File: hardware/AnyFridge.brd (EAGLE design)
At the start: 160 x 100 mm, 7 parts, among them U1 TSSP77038TT

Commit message: updated board
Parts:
- removed ESP1: ESP32, ESP32:ESP32
- removed LED1: WP154A4SUREQBFZGC, MISC-PARTS:LED4_WP154A4SUREQBFZGC_KNB
- removed S1: TS04-66-73-BK-100-SMT, MISC-PARTS:SW_TS04-66-73-BK-100-SMT
- removed SEN-1: SEN-18088, SEN-18088:SEN-18088
- removed U1: TSSP77038TT, MISC-PARTS:TSSP77038TT
- added ESP-1: ESP32, ESP32:ESP32
- added LED-1: WP154A4SUREQBFZGC, MISC-PARTS:LED4_WP154A4SUREQBFZGC_KNB
- added SCAN-1: SEN-18088, SEN-18088:SEN-18088
- added SENS-1: TSSP77038TT, MISC-PARTS:TSSP77038TT
- added SWITCH-1: TS04-66-73-BK-100-SMT, MISC-PARTS:SW_TS04-66-73-BK-100-SMT
- moved FRAME1 135.5 mm to (43.2, 2.54)
- moved R1 52.1 mm to (49.5, 3.81), turned to 0 degrees
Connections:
- removed net BUTTON: ESP1.15, S1.3
- removed net OUT: ESP1.13, U1.3
- removed net RX0: ESP1.19, SEN-1.RX
- removed net TX0: ESP1.22, SEN-1.TX
- new net RX1: ESP-1.16, SCAN-1.TX
- new net SENS-OUT: ESP-1.13, SENS-1.3
- new net SWI-OUT: ESP-1.15, SWITCH-1.3
- new net TX1: ESP-1.17, SCAN-1.RX
- net 3.3V: now also ESP-1.3V3, SCAN-1.3.3V, SENS-1.2, SWITCH-1.2; no longer ESP1.3V3, S1.2, SEN-1.3.3V, U1.2
- net BLUE: now also ESP-1.12, LED-1.3; no longer ESP1.12, LED1.3
- net GND: now also ESP-1.GND, LED-1.2, SCAN-1.GND, SENS-1.1, SENS-1.4; no longer ESP1.GND, LED1.2, SEN-1.GND, U1.1, U1.4
- net GREEN: now also ESP-1.27, LED-1.4; no longer ESP1.27, LED1.4
- net N$1: now also SWITCH-1.1; no longer S1.1
- net RED: now also ESP-1.33, LED-1.1; no longer ESP1.33, LED1.1
- net STAT: now also ESP-1.23, SCAN-1.STAT; no longer ESP1.23, SEN-1.STAT
- net TRIG: now also ESP-1.21, SCAN-1.TRIG; no longer ESP1.21, SEN-1.TRIG
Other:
- board size 160 x 100 mm -> 100 x 80 mm

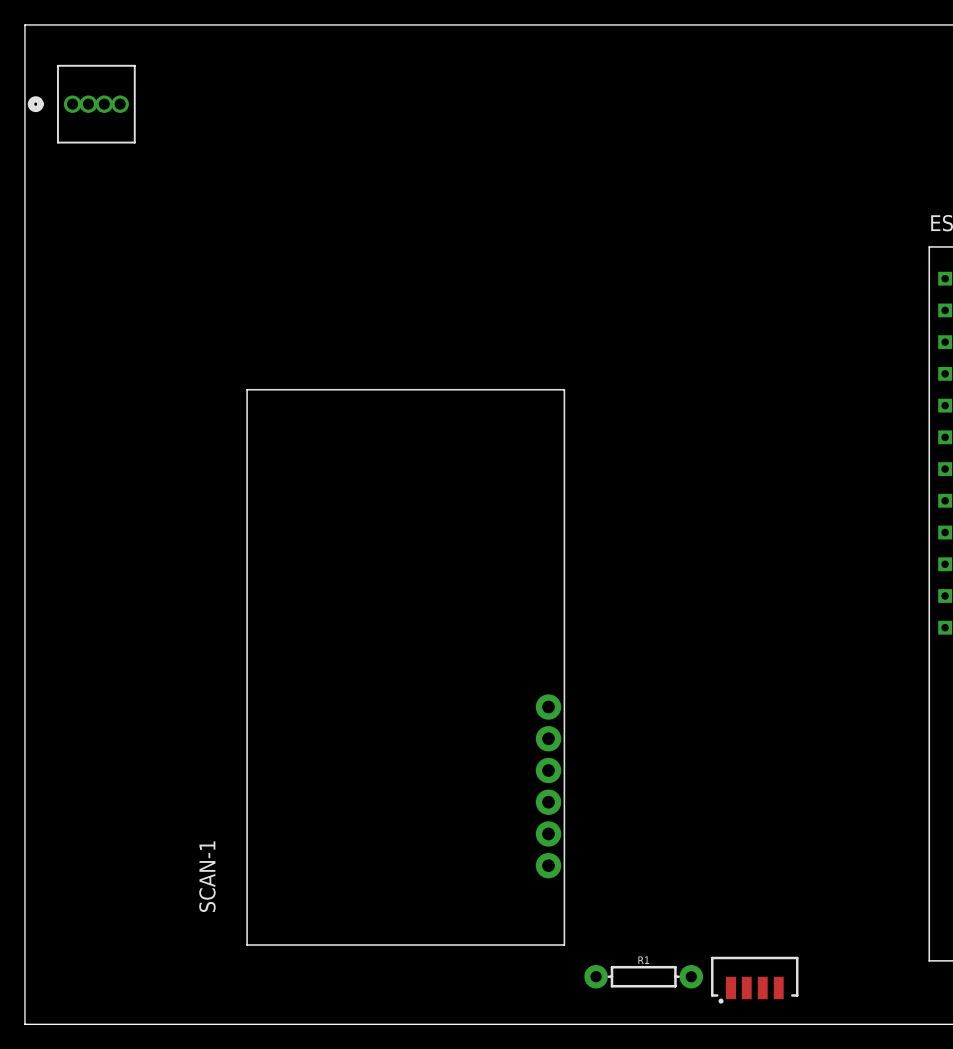
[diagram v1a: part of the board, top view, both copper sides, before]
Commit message: Rotated barcode scanner
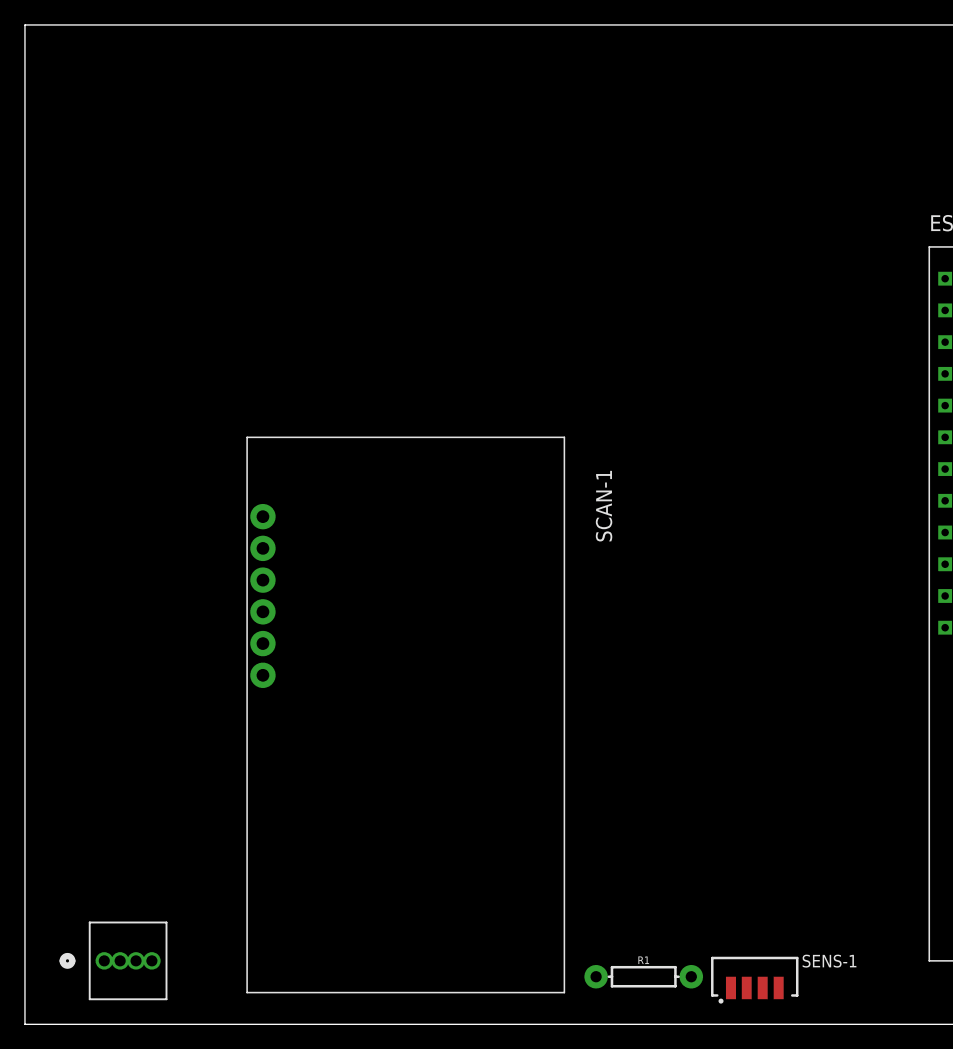
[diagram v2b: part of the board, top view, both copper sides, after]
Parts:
- moved LED-1 68.6 mm to (6.35, 5.08)
- moved SCAN-1 47.9 mm to (43.2, 47.0), turned to 270 degrees
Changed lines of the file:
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@@
 <attribute name="VERSION" value="v01" x="85.09" y="-149.86" size="1.778" layer="27" display="off"/>
 </element>
-<element name="LED-1" library="MISC-PARTS" package="LED4_WP154A4SUREQBFZGC_KNB" value="WP154A4SUREQBFZGC" x="3.81" y="73.66" smashed="yes">
-<attribute name="COPYRIGHT" value="Copyright (C) 2025 Ultra Librarian. All rights reserved." x="38.1" y="-62.23" size="1.778" layer="27" display="off"/>
-<attribute name="MANUFACTURER_PART_NUMBER" value="WP154A4SUREQBFZGC" x="38.1" y="-62.23" size="1.778" layer="27" display="off"/>
-<attribute name="MFR_NAME" value="Kingbright" x="38.1" y="-62.23" size="1.778" layer="27" display="off"/>
-<attribute name="NAME" x="2.4384" y="73.025" size="1.27" layer="27" ratio="6" rot="SR0"/>
-<attribute name="VALUE" x="3.9878" y="73.025" size="1.27" layer="27" ratio="6" rot="SR0"/>
+<element name="LED-1" library="MISC-PARTS" package="LED4_WP154A4SUREQBFZGC_KNB" value="WP154A4SUREQBFZGC" x="6.35" y="5.08" smashed="yes">
+<attribute name="COPYRIGHT" value="Copyright (C) 2025 Ultra Librarian. All rights reserved." x="40.64" y="-130.81" size="1.778" layer="27" display="off"/>
+<attribute name="MANUFACTURER_PART_NUMBER" value="WP154A4SUREQBFZGC" x="40.64" y="-130.81" size="1.778" layer="27" display="off"/>
+<attribute name="MFR_NAME" value="Kingbright" x="40.64" y="-130.81" size="1.778" layer="27" display="off"/>
+<attribute name="NAME" x="4.9784" y="4.445" size="1.27" layer="27" ratio="6" rot="SR0"/>
+<attribute name="VALUE" x="6.5278" y="4.445" size="1.27" layer="27" ratio="6" rot="SR0"/>
 </element>
 <element name="R1" library="SparkFun-Resistors" library_urn="urn:adsk.eagle:library:532" package="AXIAL-0.3" package3d_urn="urn:adsk.eagle:package:39658/2" value="10k" x="49.53" y="3.81" smashed="yes">
@@
 <attribute name="VALUE" x="49.53" y="2.794" size="0.6096" layer="27" font="vector" ratio="20" align="top-center"/>
 </element>
-<element name="SCAN-1" library="SEN-18088" package="SEN-18088" value="SEN-18088" x="17.78" y="6.35" smashed="yes" rot="R90">
-<attribute name="NAME" x="15.24" y="8.89" size="1.27" layer="25" rot="R90"/>
-<attribute name="VALUE" x="15.24" y="41.91" size="1.27" layer="27" rot="R90"/>
+<element name="SCAN-1" library="SEN-18088" package="SEN-18088" value="SEN-18088" x="43.18" y="46.99" smashed="yes" rot="R270">
+<attribute name="NAME" x="45.72" y="44.45" size="1.27" layer="25" rot="R270"/>
+<attribute name="VALUE" x="45.72" y="11.43" size="1.27" layer="27" rot="R270"/>
 </element>
 <element name="SENS-1" library="MISC-PARTS" package="TSSP77038TT" package3d_urn="urn:adsk.eagle:package:47059864/1" value="TSSP77038TT" x="58.42" y="3.81" smashed="yes">
@@
 <attribute name="MF" value="Vishay" x="85.09" y="-149.86" size="1.778" layer="27" display="off"/>
 <attribute name="MP" value="TSSP77038TT" x="85.09" y="-149.86" size="1.778" layer="27" display="off"/>
+<attribute name="NAME" x="62.17" y="4.56" size="1" layer="51" ratio="21" rot="SR0"/>
 <attribute name="NAME" x="62.17" y="4.56" size="1" layer="25" ratio="20" rot="SR0"/>
-<attribute name="NAME" x="62.17" y="4.56" size="1" layer="51" ratio="21" rot="SR0"/>
 <attribute name="PACKAGE" value="None" x="85.09" y="-149.86" size="1.778" layer="27" display="off"/>
 <attribute name="PRICE" value="None" x="85.09" y="-149.86" size="1.778" layer="27" display="off"/>
@@
 <contactref element="LED-1" pad="2"/>
 <contactref element="R1" pad="P$1"/>
+<wire x1="60.325" y1="2.91" x2="93.98" y2="29.21" width="0" layer="19" extent="1-1"/>
 <wire x1="56.515" y1="2.91" x2="60.325" y2="2.91" width="0" layer="19" extent="1-1"/>
 <wire x1="45.72" y1="3.81" x2="56.515" y2="2.91" width="0" layer="19" extent="1-1"/>
-<wire x1="5.08" y1="73.66" x2="56.515" y2="2.91" width="0" layer="19" extent="1-1"/>
-<wire x1="41.91" y1="12.7" x2="5.08" y2="73.66" width="0" layer="19" extent="1-1"/>
-<wire x1="93.98" y1="29.21" x2="41.91" y2="12.7" width="0" layer="19" extent="1-1"/>
+<wire x1="19.05" y1="40.64" x2="45.72" y2="3.81" width="0" layer="19" extent="1-1"/>
+<wire x1="7.62" y1="5.08" x2="19.05" y2="40.64" width="0" layer="19" extent="1-1"/>
 </signal>
 <signal name="3.3V">
@@
 <contactref element="SENS-1" pad="2"/>
 <contactref element="SWITCH-1" pad="2"/>
-<wire x1="76.73" y1="68.87" x2="57.785" y2="2.91" width="0" layer="19" extent="1-1"/>
-<wire x1="41.91" y1="20.32" x2="57.785" y2="2.91" width="0" layer="19" extent="1-1"/>
-<wire x1="93.98" y1="24.13" x2="41.91" y2="20.32" width="0" layer="19" extent="1-1"/>
+<wire x1="93.98" y1="24.13" x2="76.73" y2="68.87" width="0" layer="19" extent="1-1"/>
+<wire x1="57.785" y1="2.91" x2="93.98" y2="24.13" width="0" layer="19" extent="1-1"/>
+<wire x1="19.05" y1="33.02" x2="76.73" y2="68.87" width="0" layer="19" extent="1-1"/>
 </signal>
 <signal name="TRIG">
 <contactref element="SCAN-1" pad="TRIG"/>
 <contactref element="ESP-1" pad="21"/>
-<wire x1="41.91" y1="22.86" x2="93.98" y2="59.69" width="0" layer="19" extent="1-1"/>
+<wire x1="19.05" y1="30.48" x2="93.98" y2="59.69" width="0" layer="19" extent="1-1"/>
 </signal>
 <signal name="STAT">
 <contactref element="SCAN-1" pad="STAT"/>
 <contactref element="ESP-1" pad="23"/>
-<wire x1="41.91" y1="25.4" x2="73.66" y2="59.69" width="0" layer="19" extent="1-1"/>
+<wire x1="19.05" y1="27.94" x2="73.66" y2="59.69" width="0" layer="19" extent="1-1"/>
 </signal>
 <signal name="RED">
 <contactref element="LED-1" pad="1"/>
 <contactref element="ESP-1" pad="33"/>
-<wire x1="73.66" y1="46.99" x2="3.81" y2="73.66" width="0" layer="19" extent="1-1"/>
+<wire x1="73.66" y1="46.99" x2="6.35" y2="5.08" width="0" layer="19" extent="1-1"/>
 </signal>
 <signal name="BLUE">
 <contactref element="LED-1" pad="3"/>
 <contactref element="ESP-1" pad="12"/>
-<wire x1="73.66" y1="41.91" x2="6.35" y2="73.66" width="0" layer="19" extent="1-1"/>
+<wire x1="73.66" y1="41.91" x2="8.89" y2="5.08" width="0" layer="19" extent="1-1"/>
 </signal>
 <signal name="GREEN">
 <contactref element="LED-1" pad="4"/>
 <contactref element="ESP-1" pad="27"/>
-<wire x1="73.66" y1="44.45" x2="7.62" y2="73.66" width="0" layer="19" extent="1-1"/>
+<wire x1="73.66" y1="44.45" x2="10.16" y2="5.08" width="0" layer="19" extent="1-1"/>
 </signal>
 <signal name="N$1">
@@
 <contactref element="ESP-1" pad="17"/>
 <contactref element="SCAN-1" pad="RX"/>
-<wire x1="41.91" y1="15.24" x2="93.98" y2="57.15" width="0" layer="19" extent="1-1"/>
+<wire x1="19.05" y1="38.1" x2="93.98" y2="57.15" width="0" layer="19" extent="1-1"/>
 </signal>
 <signal name="RX1">
 <contactref element="ESP-1" pad="16"/>
 <contactref element="SCAN-1" pad="TX"/>
-<wire x1="41.91" y1="17.78" x2="93.98" y2="54.61" width="0" layer="19" extent="1-1"/>
+<wire x1="19.05" y1="35.56" x2="93.98" y2="54.61" width="0" layer="19" extent="1-1"/>
 </signal>
 <signal name="SWI-OUT">

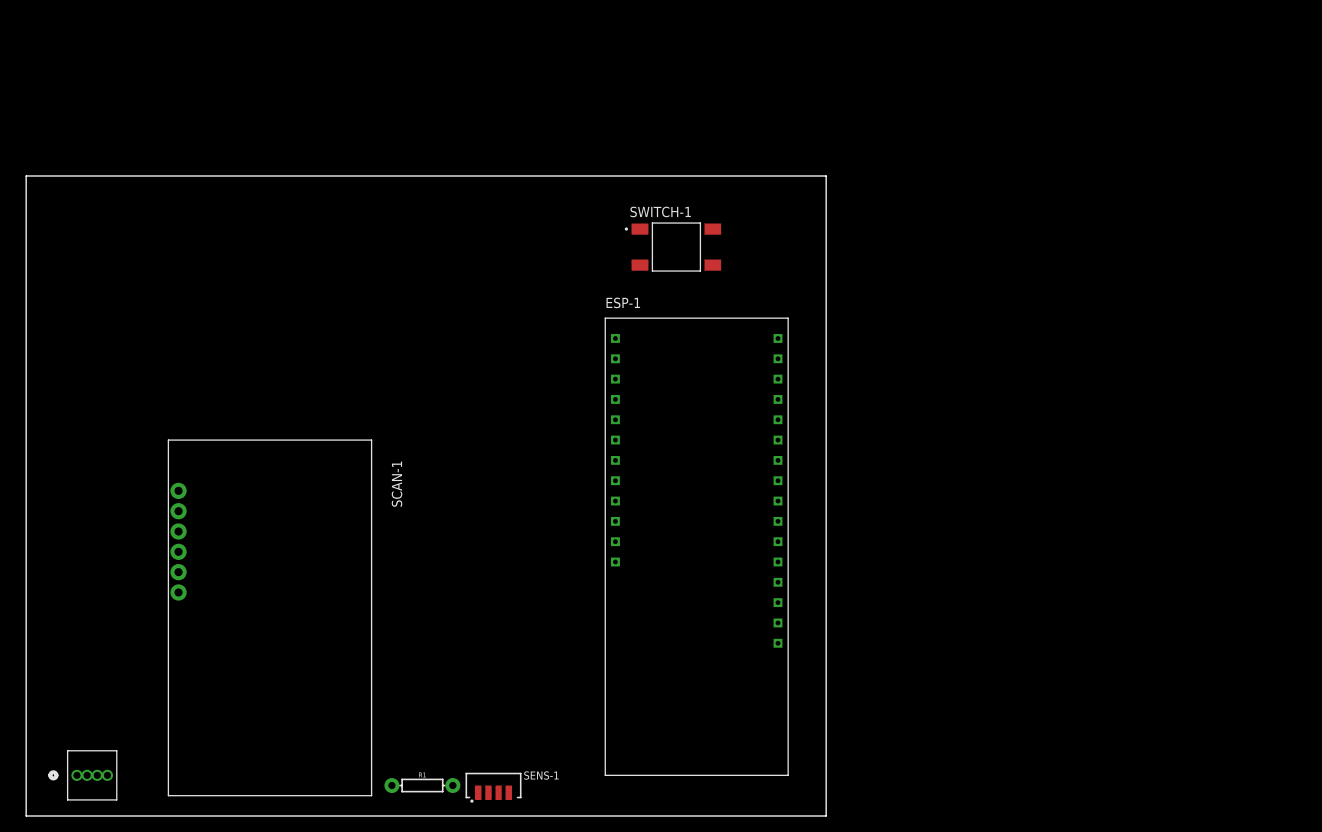
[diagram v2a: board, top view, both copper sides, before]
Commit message: Add GND copper pour on top layer
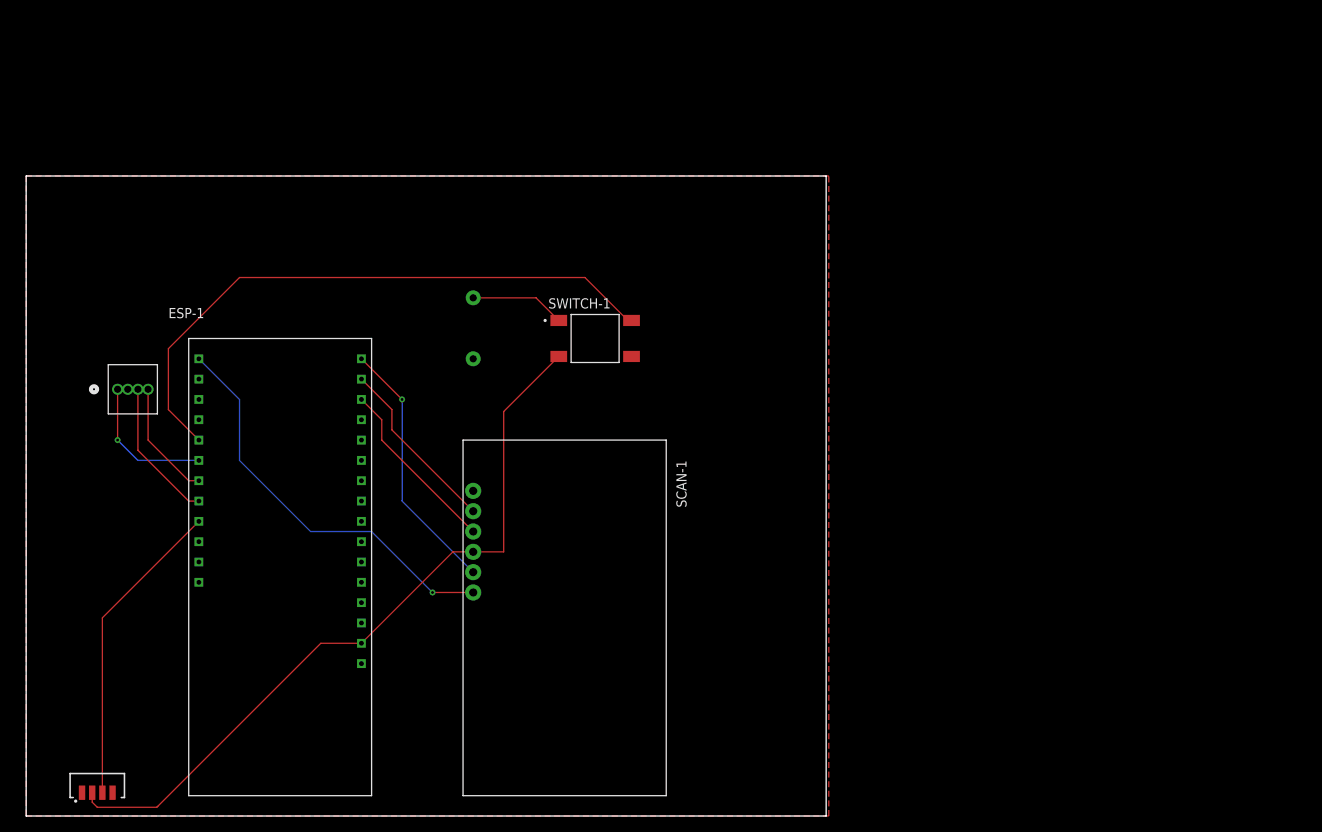
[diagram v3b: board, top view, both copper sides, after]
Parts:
- moved R1 57.5 mm to (55.9, 61.0), flipped to the bottom, turned to 90 degrees
- moved ESP-1 52.1 mm to (20.3, 2.54)
- moved SENS-1 49.5 mm to (8.89, 3.81)
- moved LED-1 48.5 mm to (11.4, 53.3)
- moved SCAN-1 36.8 mm to (80.0, 47.0)
- moved SWITCH-1 15.3 mm to (71.1, 59.7)
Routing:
- net 3.3V: track 0.00 -> 93.4 mm
- net SWI-OUT: track 0.00 -> 76.8 mm
- net STAT: track 0.00 -> 50.9 mm, vias 0 -> 1
- net SENS-OUT: track 0.00 -> 38.9 mm
- net TRIG: track 0.00 -> 32.5 mm, vias 0 -> 1
- net TX1: track 0.00 -> 22.3 mm
- net RX1: track 0.00 -> 22.3 mm
- net BLUE: track 0.00 -> 17.9 mm
- net RED: track 0.00 -> 17.6 mm, vias 0 -> 1
- net GREEN: track 0.00 -> 14.8 mm
- net N$1: track 0.00 -> 11.9 mm
- added copper zone on layer 1, net GND

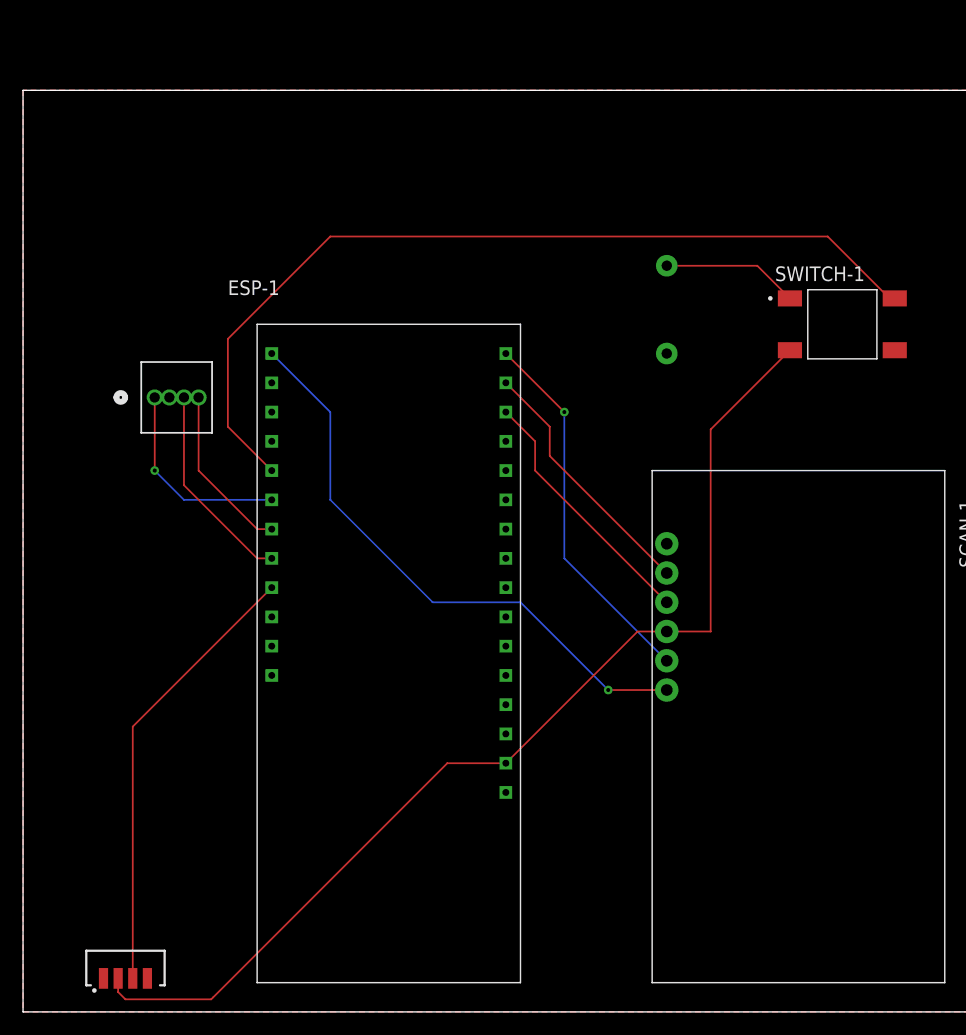
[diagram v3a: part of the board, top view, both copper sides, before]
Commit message: Increase traces to 16mm and add test points for UART
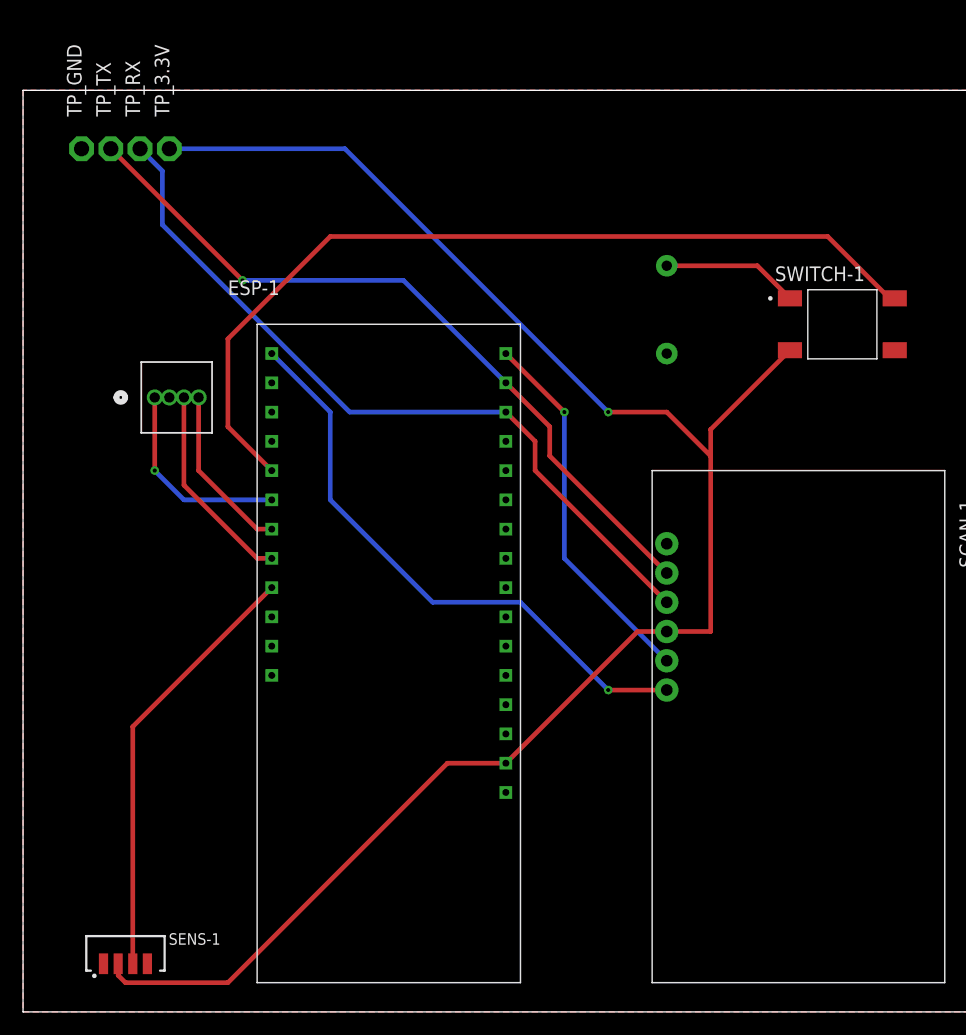
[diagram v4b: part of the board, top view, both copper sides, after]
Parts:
- added TP_3.3V, TP_GND, TP_RX, TP_TX: TPPAD1-13, testpad:P1-13
- moved SENS-1 1.27 mm to (8.89, 5.08)
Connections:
- net 3.3V: now also TP_3.3V.TP
- net GND: now also TP_GND.TP
- net RX1: now also TP_RX.TP
- net TX1: now also TP_TX.TP
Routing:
- net 3.3V: track 93.4 -> 150.6 mm, vias 0 -> 1
- net RX1: track 22.3 -> 66.3 mm
- net TX1: track 22.3 -> 65.0 mm, vias 0 -> 1
- net SENS-OUT: track 38.9 -> 37.6 mm
